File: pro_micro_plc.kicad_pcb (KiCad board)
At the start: 2 copper layers, 75 x 50 mm, 39 parts, among them J1 Conn_01x06_Pin, J2 Conn_01x02_Socket, J3 Conn_01x02_Socket, J4 Conn_01x02_Socket, J5 Conn_01x02_Pin, J6 Conn_01x04_Pin, Q1 2N7002K, Q2 2N7002K, Q3 2N7002K, Q4 2N7002K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

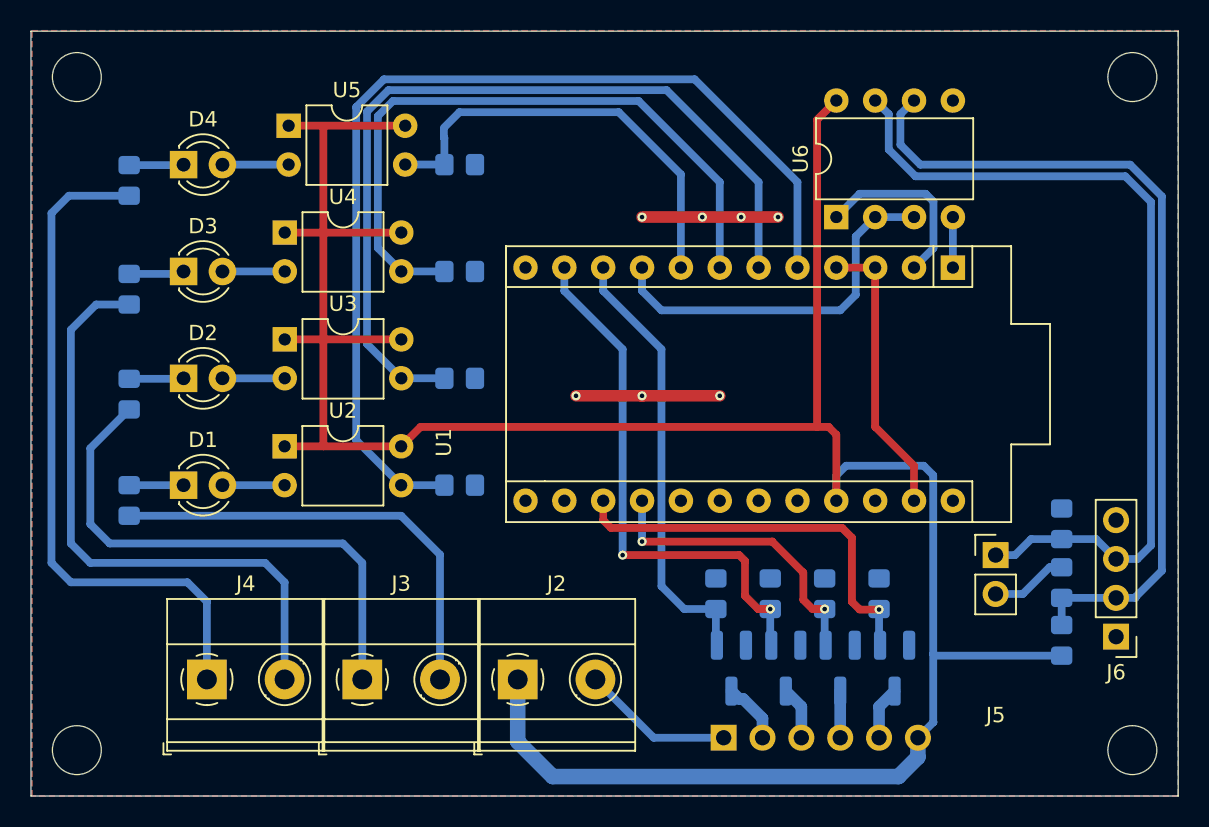
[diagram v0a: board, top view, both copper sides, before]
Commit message: add analog input
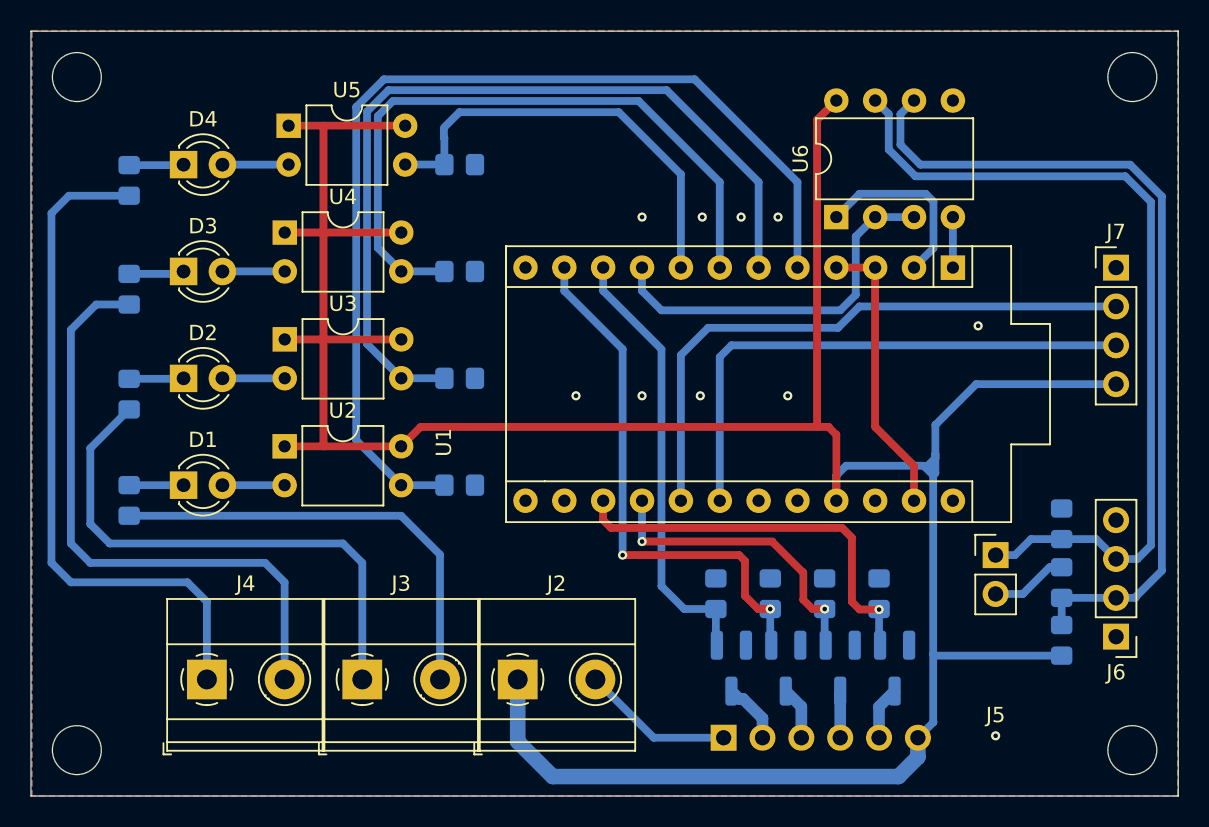
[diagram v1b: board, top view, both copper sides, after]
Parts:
- added J7: Conn_01x04_Pin, Connector_PinHeader_2.54mm:PinHeader_1x04_P2.54mm_Vertical, F.Cu at (113.3, 34.0)
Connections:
- U1 pad 17: unconnected-(U1-D18/A0-Pad17) -> /IW0.0
- U1 pad 18: unconnected-(U1-D19/A1-Pad18) -> /IW0.1
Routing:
- net /IW0.0: track 0.00 -> 39.3 mm
- net /IW0.1: track 0.00 -> 35.6 mm
- net GND: track 47.1 -> 28.8 mm, vias 7 -> 10
- net +5V: track 174.3 -> 191.7 mm

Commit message: smallest PCB
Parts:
- moved R1 27.0 mm to (71.6, 48.8)
- moved R15 26.8 mm to (106.6, 31.8), turned to 90 degrees
- moved R3 26.6 mm to (69.1, 39.9), turned to 90 degrees
- moved J5 22.1 mm to (97.0, 32.4), turned to -90 degrees
- moved R4 21.9 mm to (71.6, 39.9), turned to 90 degrees
- moved R2 21.1 mm to (74.2, 48.8)
- moved J6 20.1 mm to (114.2, 38.1)
- moved J7 18.1 mm to (114.2, 52.1)
- moved R5 16.3 mm to (84.3, 39.9), turned to -90 degrees
- moved R8 14.1 mm to (76.7, 39.9), turned to -90 degrees
- moved R14 14.0 mm to (106.6, 37.1), turned to 90 degrees
- moved R9 13.1 mm to (106.6, 41.9), turned to -90 degrees
- moved R6 11.5 mm to (81.8, 39.9), turned to -90 degrees
- moved R7 10.5 mm to (79.2, 39.9), turned to -90 degrees
- moved U1 8.59 mm to (66.5, 52.1)
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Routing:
- net /Bus+: track 55.3 -> 18.7 mm, vias 0 -> 1
- net /Bus-: track 56.1 -> 22.0 mm
- net /IX0.0: track 66.7 -> 37.2 mm
- net /IX0.1: track 55.4 -> 29.0 mm
- net /QX0.0: track 28.5 -> 53.5 mm
- net /IX0.2: track 44.2 -> 25.2 mm
- net Net-(J5-Pin_2): track 5.04 -> 20.1 mm
- net /QX0.1: track 35.0 -> 49.7 mm, vias 2 -> 0
- net GND: track 28.8 -> 15.7 mm, vias 10 -> 9
- net /DE: track 24.6 -> 34.8 mm
- net Net-(J4-Pin_1): track 44.8 -> 36.0 mm
- net /QX0.3: track 20.4 -> 27.7 mm, vias 2 -> 1
- net /IW0.1: track 35.6 -> 42.3 mm
- net /QX0.2: track 26.6 -> 33.2 mm, vias 1 -> 0
- net Net-(J4-Pin_2): track 40.0 -> 33.4 mm
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
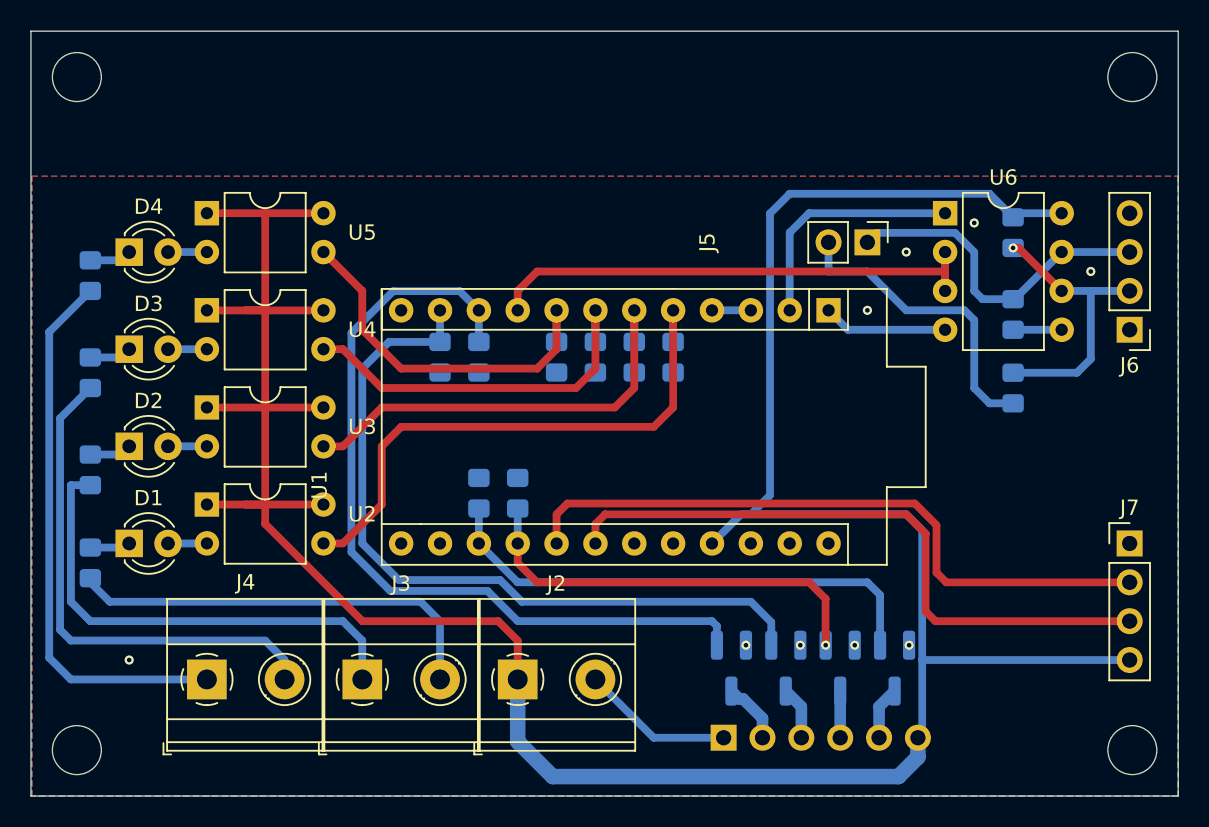
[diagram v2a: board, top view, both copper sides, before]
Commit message: more space for max485 and vias on ground
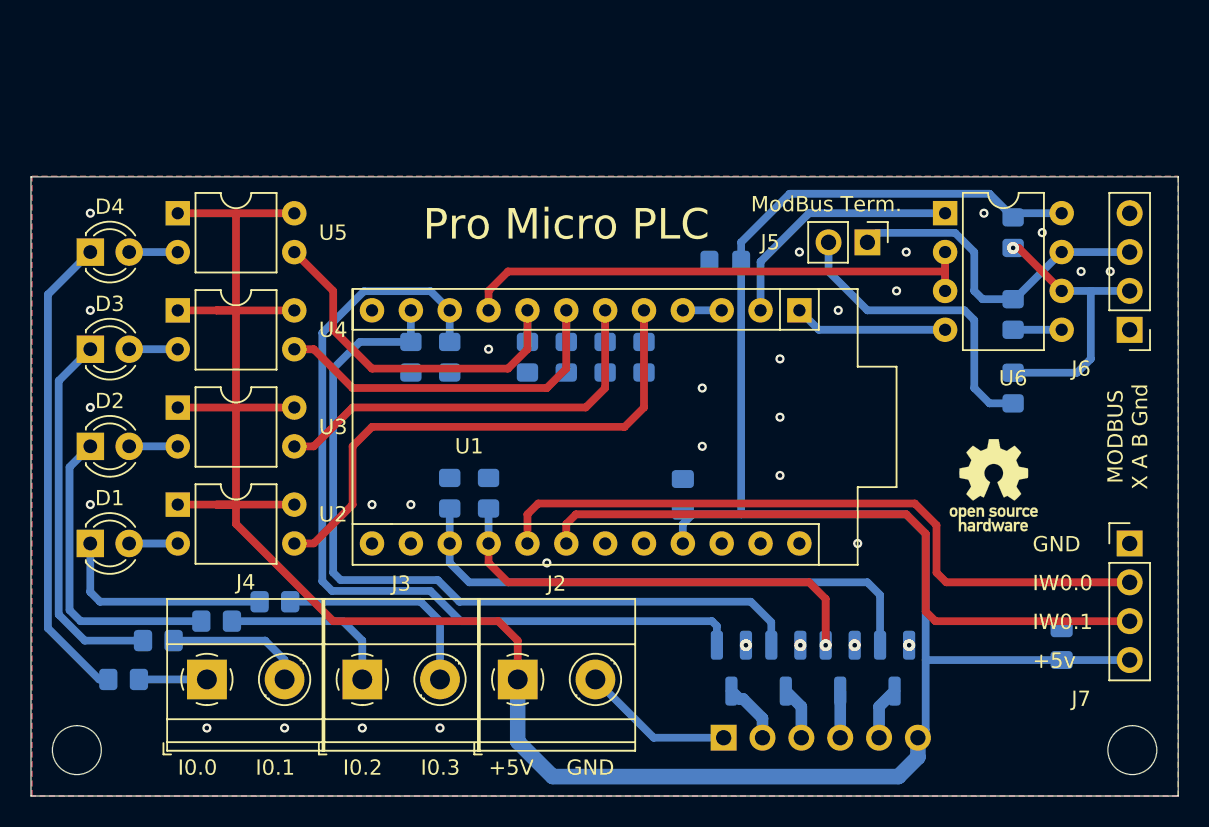
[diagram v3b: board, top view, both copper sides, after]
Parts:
- removed the REF** at (114.3, 21.6)
- removed the REF** at (45.3, 21.6)
- added C1: 100nF, Capacitor_SMD:C_0805_2012Metric_Pad1.18x1.45mm_HandSolder, B.Cu at (87.7, 33.7)
- added C2: 100nF, Capacitor_SMD:C_0805_2012Metric_Pad1.18x1.45mm_HandSolder, B.Cu at (85.0, 48.9)
- added C3: 100nF, Capacitor_SMD:C_0805_2012Metric_Pad1.18x1.45mm_HandSolder, B.Cu at (109.7, 58.7)
- added REF**: OSHW-Logo_5.7x6mm_SilkScreen, Symbol:OSHW-Logo_5.7x6mm_SilkScreen, F.Cu at (105.3, 48.3)
- moved R13 26.5 mm to (48.4, 61.0), turned to 0 degrees
- moved R12 18.1 mm to (50.7, 58.4), turned to 0 degrees
- moved R11 12.9 mm to (54.5, 57.1), turned to 0 degrees
- moved R10 12.3 mm to (58.3, 55.9), turned to 0 degrees
- moved D1 2.55 mm to (46.2, 52.1)
- moved D2 2.54 mm to (46.2, 45.7)
- moved D3 2.54 mm to (46.2, 39.4)
- moved D4 2.54 mm to (46.2, 33.0)
- moved U2 1.91 mm to (51.9, 49.5)
- moved U3 1.91 mm to (51.9, 43.2)
- moved U4 1.91 mm to (51.9, 36.8)
- moved U5 1.91 mm to (51.9, 30.5)
- moved R1 1.91 mm to (69.7, 48.8)
- moved R2 1.91 mm to (72.3, 48.8)
- moved R4 1.91 mm to (69.7, 39.9)
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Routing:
- net Net-(J4-Pin_1): track 36.0 -> 4.45 mm
- net Net-(D4-Pad1): track 2.76 -> 31.1 mm
- net Net-(J4-Pin_2): track 33.4 -> 9.05 mm
- net Net-(D3-Pad1): track 2.76 -> 24.4 mm
- net Net-(J3-Pin_1): track 31.5 -> 11.6 mm
- net Net-(D2-Pad1): track 2.76 -> 20.2 mm
- net Net-(J3-Pin_2): track 28.0 -> 14.1 mm
- net Net-(D1-Pad1): track 2.65 -> 14.5 mm
- net +5V: track 190.9 -> 195.6 mm
- net /QX0.1: track 49.7 -> 52.7 mm
- net /QX0.0: track 53.5 -> 56.5 mm
- net /QX0.2: track 33.2 -> 35.8 mm
- net /TXD1: track 8.15 -> 10.1 mm
- net /QX0.3: track 27.7 -> 29.6 mm
- net /IW0.1: track 42.3 -> 44.2 mm
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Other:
- board size 75 x 50 mm -> 75 x 40.5 mm
- board text added: "+5V"
- board text added: "+5v"
- board text added: "GND"
- board text added: "I0.0"
- board text added: "I0.1"
- board text added: "I0.2"
- board text added: "I0.3"
- board text added: "IW0.0"
- board text added: "IW0.1"
- board text added: "MODBUS X A B Gnd"
- board text added: "ModBus Term."
- board text added: "Pro Micro PLC"

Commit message: update terminal blocks
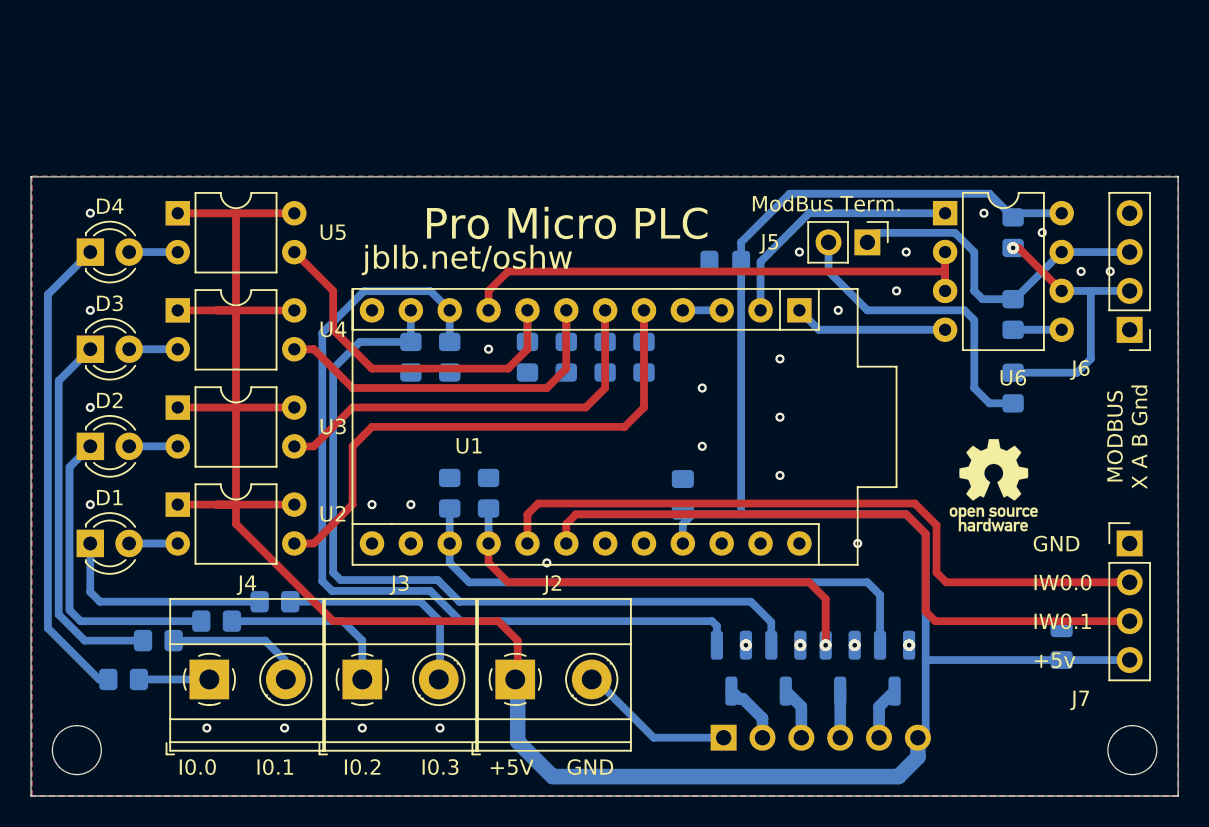
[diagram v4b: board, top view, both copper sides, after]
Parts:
- J2, J3, J4: footprint TerminalBlock_Phoenix:TerminalBlock_Phoenix_MKDS-1,5-2-5.08_1x02_P5.08mm_Horizontal -> TerminalBlock_Phoenix:TerminalBlock_Phoenix_MKDS-1,5-2_1x02_P5.00mm_Horizontal
- moved J2 0.16 mm to (74.0, 61.0)
- moved J4 0.16 mm to (54.0, 61.0)
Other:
- board text added: "jblb.net/oshw"

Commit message: Update README
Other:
- board text added: "Outputs 0..3"
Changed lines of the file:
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@@
+		)
+	)
+	(gr_text "Outputs 0..3"
+		(at 89.408 62.738 0)
+		(layer "F.SilkS")
+		(effects
+			(font
+				(size 1 1)
+				(thickness 0.15)
+			)
+			(justify left bottom)
 		)
 	)
@@
 		(layer "F.SilkS")
 		(effects
+			(font
+				(size 1 1)
+				(thickness 0.15)
+			)
+			(justify left bottom)
+		)
+	)
+	(gr_text "+5V"
+		(at 99.568 62.738 0)
+		(layer "F.SilkS")
+		(effects
+			(font
+				(size 1 1)
+				(thickness 0.15)
+			)
+			(justify left bottom)
+		)
+	)
+	(gr_text "GND"
+		(at 85.598 62.738 0)
+		(layer "F.SilkS")
+		(effects
